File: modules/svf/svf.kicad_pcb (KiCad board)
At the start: 2 copper layers, 30.5 x 68.6 mm, 4 parts

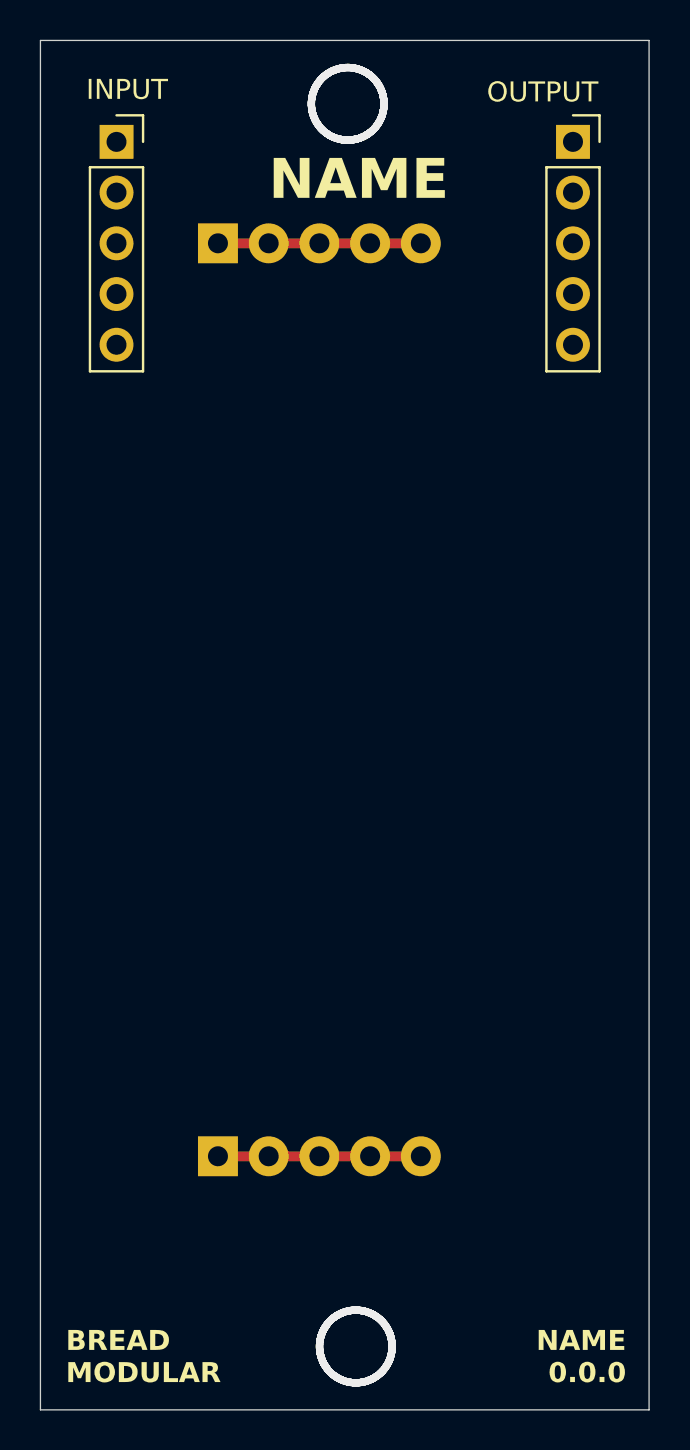
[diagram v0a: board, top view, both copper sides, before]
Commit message: Finalized the PCB routing
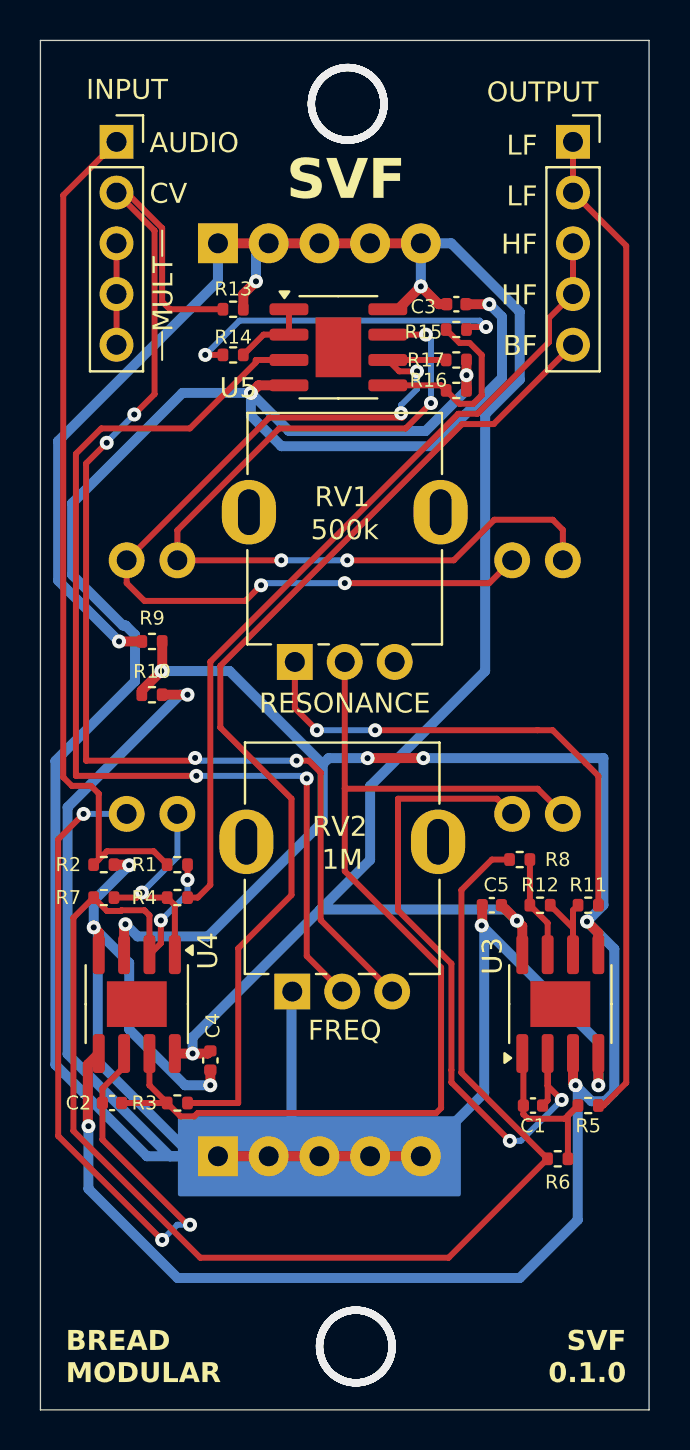
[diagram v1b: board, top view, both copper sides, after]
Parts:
- added C1: 10nf, Capacitor_SMD:C_0402_1005Metric, F.Cu at (71.7, 94.0)
- added C2: 10nf, Capacitor_SMD:C_0402_1005Metric, F.Cu at (50.6, 93.9)
- added C3: 0.1uf, Capacitor_SMD:C_0402_1005Metric, F.Cu at (67.8, 53.8)
- added C4: 0.1uf, Capacitor_SMD:C_0402_1005Metric, F.Cu at (55.5, 91.7)
- added C5: 0.1uf, Capacitor_SMD:C_0402_1005Metric, F.Cu at (69.6, 83.9)
- added R1: 100k, Resistor_SMD:R_0402_1005Metric, F.Cu at (53.8, 81.9)
- added R10: 1k, Resistor_SMD:R_0402_1005Metric, F.Cu at (52.6, 73.4)
- added R11: 10k, Resistor_SMD:R_0402_1005Metric, F.Cu at (74.4, 83.9)
- added R12: 10k, Resistor_SMD:R_0402_1005Metric, F.Cu at (72.0, 83.9)
- added R13: 100k, Resistor_SMD:R_0402_1005Metric, F.Cu at (56.6, 54.1)
- added R14: 1k, Resistor_SMD:R_0402_1005Metric, F.Cu at (56.6, 56.4)
- added R15: 1M, Resistor_SMD:R_0402_1005Metric, F.Cu at (67.8, 55.1)
- added R16: 1M, Resistor_SMD:R_0402_1005Metric, F.Cu at (67.8, 58.2)
- added R17: 10k, Resistor_SMD:R_0402_1005Metric, F.Cu at (67.8, 56.6)
- added R2: 22k, Resistor_SMD:R_0402_1005Metric, F.Cu at (50.2, 81.9)
- added R3: 1k, Resistor_SMD:R_0402_1005Metric, F.Cu at (53.8, 93.9)
- added R4: 1k, Resistor_SMD:R_0402_1005Metric, F.Cu at (53.8, 83.6)
- added R5: 1k, Resistor_SMD:R_0402_1005Metric, F.Cu at (74.4, 94.0)
- added R6: 10k, Resistor_SMD:R_0402_1005Metric, F.Cu at (72.9, 96.6)
- added R7: 10k, Resistor_SMD:R_0402_1005Metric, F.Cu at (50.2, 83.6)
- added R8: 10k, Resistor_SMD:R_0402_1005Metric, F.Cu at (71.0, 81.7)
- added R9: 1k, Resistor_SMD:R_0402_1005Metric, F.Cu at (52.6, 70.7)
- added RV1: 500k, BreadModular_Pots:Potentiometer_RV09, F.Cu at (62.4, 64.8)
- added RV2: 1M, BreadModular_Pots:Potentiometer_RV09, F.Cu at (62.2, 81.3)
- added U1: VTL5C, BreadModular_MISC:VTL5C, B.Cu at (71.9, 73.0)
- added U2: VTL5C, BreadModular_MISC:VTL5C, B.Cu at (52.6, 73.0)
- added U3: MCP6002-xSN, Package_SO:SOIC-8-1EP_3.9x4.9mm_P1.27mm_EP2.29x3mm, F.Cu at (73.0, 88.9)
- added U4: MCP6002-xSN, Package_SO:SOIC-8-1EP_3.9x4.9mm_P1.27mm_EP2.29x3mm, F.Cu at (51.8, 88.9)
- added U5: MCP6002-xSN, Package_SO:SOIC-8-1EP_3.9x4.9mm_P1.27mm_EP2.29x3mm, F.Cu at (61.9, 56.0)
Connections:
- INPUT1 pad 1: unconnected-(INPUT1-Pin_1-Pad1) -> V_IN
- INPUT1 pad 2: unconnected-(INPUT1-Pin_2-Pad2) -> V_CV
- INPUT1 pad 3: unconnected-(INPUT1-Pin_3-Pad3) -> Net-(INPUT1-Pin_3)
- INPUT1 pad 4: unconnected-(INPUT1-Pin_4-Pad4) -> Net-(INPUT1-Pin_3)
- INPUT1 pad 5: unconnected-(INPUT1-Pin_5-Pad5) -> Net-(INPUT1-Pin_3)
- OUTPUT1 pad 1: unconnected-(OUTPUT1-Pin_1-Pad1) -> V_LF
- OUTPUT1 pad 2: unconnected-(OUTPUT1-Pin_2-Pad2) -> V_LF
- OUTPUT1 pad 3: unconnected-(OUTPUT1-Pin_3-Pad3) -> V_HF
- OUTPUT1 pad 4: unconnected-(OUTPUT1-Pin_4-Pad4) -> V_HF
- OUTPUT1 pad 5: unconnected-(OUTPUT1-Pin_5-Pad5) -> V_BF
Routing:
- net GND: track 10.2 -> 199.3 mm, vias 0 -> 9
- net V_MID: track 0.00 -> 109.2 mm, vias 0 -> 7
- net V_SUPPLY: track 10.2 -> 110.7 mm, vias 0 -> 5
- net Net-(U4A--): track 0.00 -> 69.3 mm, vias 0 -> 2
- net V_CV: track 0.00 -> 65.1 mm, vias 0 -> 4
- net Net-(C2-Pad2): track 0.00 -> 55.1 mm
- net Net-(U5A-+): track 0.00 -> 51.8 mm, vias 0 -> 2
- net V_BF: track 0.00 -> 51.3 mm
- net V_LF: track 0.00 -> 50.1 mm
- net VACTROL_NEG: track 0.00 -> 45.7 mm, vias 0 -> 4
- net VACTROL_POS: track 0.00 -> 44.2 mm, vias 0 -> 4
- net V_IN: track 0.00 -> 42.9 mm
- net V_HF: track 0.00 -> 41.6 mm
- net Net-(U4B--): track 0.00 -> 38.8 mm, vias 0 -> 3
- net Net-(U3A--): track 0.00 -> 34.3 mm, vias 0 -> 2
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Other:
- board text added: "AUDIO"
- board text added: "BF"
- board text added: "CV"
- board text added: "FREQ"
- board text added: "HF"
- board text added: "LF"
- board text added: "MULT"
- board text added: "RESONANCE"
- board text added: "SVF"
- board text added: "SVF 0.1.0"
- board text removed: "NAME"
- board text removed: "NAME 0.0.0"

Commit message: svf: make it louder & add curve control Now the SVF is 8db louder in general. Now the resonance control active troughout the potentiometer Add the curve support for the freq so, we can target low or high based on the usage.
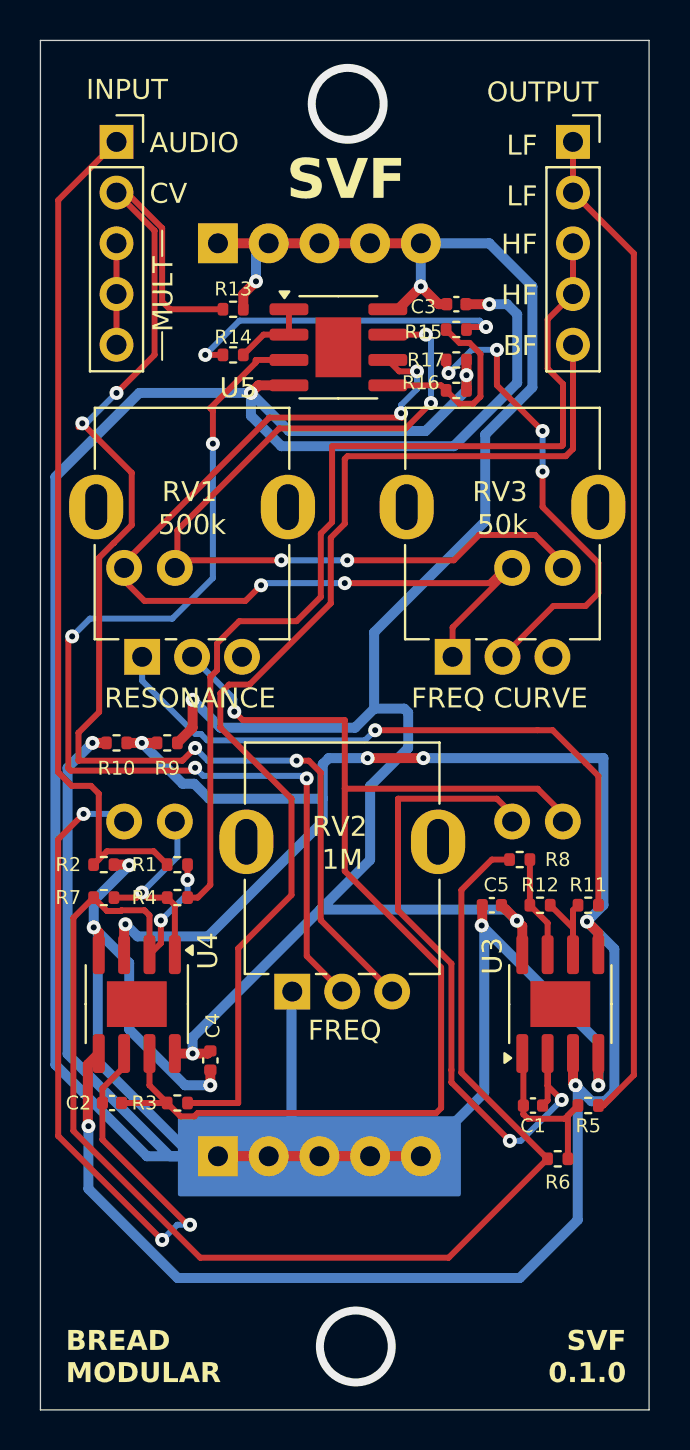
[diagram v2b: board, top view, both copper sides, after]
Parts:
- added RV3: 50k, BreadModular_Pots:Potentiometer_RV09, F.Cu at (70.3, 64.5)
- R1: value 100k -> 51k
- R11, R12: value 10k -> 51k
- R17: value 10k -> 5.1k
- moved RV1 7.65 mm to (54.7, 64.5)
- moved R9 5.14 mm to (53.3, 75.8), turned to 180 degrees
- moved R10 2.99 mm to (50.8, 75.8), turned to 180 degrees
- moved U2 0.40 mm to (52.5, 73.4)
- moved U1 0.38 mm to (71.9, 73.4)
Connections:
- R17 pad 2: VACTROL_NEG -> Net-(R17-Pad2)
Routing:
- net Net-(R17-Pad2): track 0.00 -> 24.0 mm, vias 0 -> 4
- net V_SUPPLY: track 110.7 -> 101.5 mm
- net V_HF: track 41.6 -> 50.1 mm
- net Net-(R11-Pad2): track 25.4 -> 32.9 mm, vias 2 -> 1
- net Net-(C2-Pad2): track 55.1 -> 61.5 mm, vias 0 -> 1
- net V_BF: track 51.3 -> 57.4 mm
- net GND: track 199.3 -> 194.4 mm
- net V_CV: track 65.1 -> 68.5 mm
- net VACTROL_NEG: track 45.7 -> 48.5 mm
- net VACTROL_POS: track 44.2 -> 42.6 mm
- net V_MID: track 109.2 -> 107.9 mm
- net Net-(U5A-+): track 51.8 -> 52.2 mm, vias 2 -> 4
- net (no net): vias 8 -> 2
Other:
- board text added: "FREQ CURVE"

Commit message: svf: add production files for 0.2.0
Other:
- board text added: "SVF 0.2.0"
- board text removed: "SVF 0.1.0"
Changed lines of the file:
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@@
 		)
 	)
-	(gr_text "SVF\n0.1.0"
+	(gr_text "SVF\n0.2.0"
 		(at 76.327 107.95 0)
 		(layer "F.SilkS")
